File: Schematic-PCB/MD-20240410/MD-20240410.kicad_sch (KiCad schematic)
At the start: 49 parts, among them J1 Conn_01x05_Pin, J2 Conn_01x04_Pin, J3 Conn_01x02_Pin, J4 Conn_01x02_Pin, J5 Conn_01x02_Pin, J6 Conn_01x02_Pin, J7 Conn_01x02_Pin, J8 Conn_01x15_Pin, Q3 NMOS, Q4 NMOS

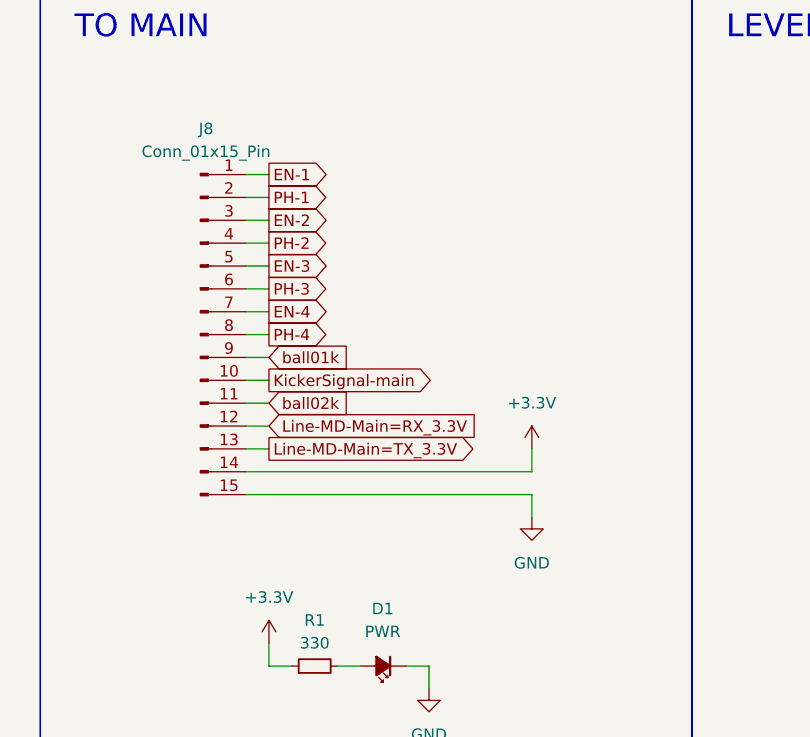
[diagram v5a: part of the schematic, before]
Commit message: FPC/FCCコネクタの順番を変更した
斜めに挿入・逆向きに挿入したときに+3.3VとGNDがショートしないようにした
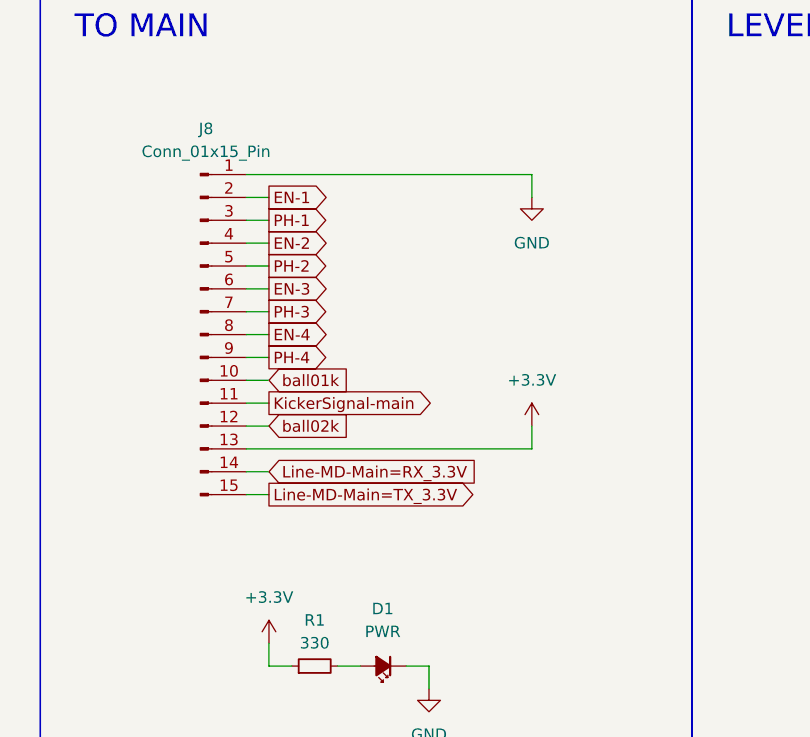
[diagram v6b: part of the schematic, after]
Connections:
- net +3.3V: now also J8.13 (Pin_13); no longer J8.14 (Pin_14)
- net EN-1: now also J8.2 (Pin_2); no longer J8.1 (Pin_1)
- net EN-2: now also J8.4 (Pin_4); no longer J8.3 (Pin_3)
- net EN-3: now also J8.6 (Pin_6); no longer J8.5 (Pin_5)
- net EN-4: now also J8.8 (Pin_8); no longer J8.7 (Pin_7)
- net GND: now also J8.1 (Pin_1); no longer J8.15 (Pin_15)
- net KickerSignal-main: now also J8.11 (Pin_11); no longer J8.10 (Pin_10)
- net Line-MD-Main=RX_3.3V: now also J8.14 (Pin_14); no longer J8.12 (Pin_12)
- net Line-MD-Main=TX_3.3V: now also J8.15 (Pin_15); no longer J8.13 (Pin_13)
- net PH-1: now also J8.3 (Pin_3); no longer J8.2 (Pin_2)
- net PH-2: now also J8.5 (Pin_5); no longer J8.4 (Pin_4)
- net PH-3: now also J8.7 (Pin_7); no longer J8.6 (Pin_6)
- net PH-4: now also J8.9 (Pin_9); no longer J8.8 (Pin_8)
- net ball01k: now also J8.10 (Pin_10); no longer J8.9 (Pin_9)
- net ball02k: now also J8.12 (Pin_12); no longer J8.11 (Pin_11)
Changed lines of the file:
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@@
 	(wire
 		(pts
-			(xy 107.95 179.07) (xy 110.49 179.07)
+			(xy 107.95 181.61) (xy 110.49 181.61)
 		)
 		(stroke
@@
 	(wire
 		(pts
-			(xy 110.49 194.31) (xy 107.95 194.31)
+			(xy 110.49 199.39) (xy 107.95 199.39)
 		)
 		(stroke
@@
 	(wire
 		(pts
-			(xy 107.95 186.69) (xy 110.49 186.69)
+			(xy 107.95 189.23) (xy 110.49 189.23)
 		)
 		(stroke
@@
 	(wire
 		(pts
-			(xy 110.49 166.37) (xy 107.95 166.37)
+			(xy 110.49 168.91) (xy 107.95 168.91)
 		)
 		(stroke
@@
 	(wire
 		(pts
-			(xy 110.49 191.77) (xy 107.95 191.77)
+			(xy 110.49 196.85) (xy 107.95 196.85)
 		)
 		(stroke
@@
 	(wire
 		(pts
-			(xy 107.95 173.99) (xy 110.49 173.99)
+			(xy 107.95 176.53) (xy 110.49 176.53)
 		)
 		(stroke
@@
 	(wire
 		(pts
-			(xy 107.95 168.91) (xy 110.49 168.91)
+			(xy 107.95 171.45) (xy 110.49 171.45)
 		)
 		(stroke
@@
 	(wire
 		(pts
-			(xy 107.95 171.45) (xy 110.49 171.45)
+			(xy 107.95 173.99) (xy 110.49 173.99)
 		)
 		(stroke
@@
 	(wire
 		(pts
-			(xy 107.95 196.85) (xy 139.7 196.85)
+			(xy 107.95 194.31) (xy 139.7 194.31)
 		)
 		(stroke
@@
 	(wire
 		(pts
-			(xy 107.95 184.15) (xy 110.49 184.15)
+			(xy 107.95 186.69) (xy 110.49 186.69)
 		)
 		(stroke
@@
 	(wire
 		(pts
-			(xy 107.95 199.39) (xy 139.7 199.39)
+			(xy 107.95 163.83) (xy 139.7 163.83)
 		)
 		(stroke
@@
 	(wire
 		(pts
-			(xy 139.7 201.93) (xy 139.7 199.39)
+			(xy 139.7 166.37) (xy 139.7 163.83)
 		)
 		(stroke
@@
 	(wire
 		(pts
-			(xy 107.95 176.53) (xy 110.49 176.53)
+			(xy 107.95 179.07) (xy 110.49 179.07)
 		)
 		(stroke
@@
 	(wire
 		(pts
-			(xy 110.49 163.83) (xy 107.95 163.83)
+			(xy 110.49 166.37) (xy 107.95 166.37)
 		)
 		(stroke
@@
 	(wire
 		(pts
-			(xy 107.95 181.61) (xy 110.49 181.61)
+			(xy 107.95 184.15) (xy 110.49 184.15)
 		)
 		(stroke
@@
 	(wire
 		(pts
-			(xy 139.7 196.85) (xy 139.7 194.31)
+			(xy 139.7 194.31) (xy 139.7 191.77)
 		)
 		(stroke
@@
 	(wire
 		(pts
-			(xy 110.49 189.23) (xy 107.95 189.23)
+			(xy 110.49 191.77) (xy 107.95 191.77)
 		)
 		(stroke
@@
 	(global_label "EN-2"
 		(shape output)
-		(at 110.49 168.91 0)
+		(at 110.49 171.45 0)
 		(fields_autoplaced yes)
 		(effects
@@
 		)
 		(property "Intersheetrefs" "${INTERSHEET_REFS}"
-			(at 118.7366 168.91 0)
+			(at 118.7366 171.45 0)
 			(effects
 				(font
@@
 	(global_label "ball02k"
 		(shape input)
-		(at 110.49 189.23 0)
+		(at 110.49 191.77 0)
 		(fields_autoplaced yes)
 		(effects
@@
 		)
 		(property "Intersheetrefs" "${INTERSHEET_REFS}"
-			(at 120.5507 189.23 0)
+			(at 120.5507 191.77 0)
 			(effects
 				(font
@@
 	(global_label "ball01k"
 		(shape input)
-		(at 110.49 184.15 0)
+		(at 110.49 186.69 0)
 		(fields_autoplaced yes)
 		(effects
@@
 		)
 		(property "Intersheetrefs" "${INTERSHEET_REFS}"
-			(at 120.5507 184.15 0)
+			(at 120.5507 186.69 0)
 			(effects
 				(font
@@
 	(global_label "Line-MD-Main=RX_3.3V"
 		(shape input)
-		(at 110.49 191.77 0)
+		(at 110.49 196.85 0)
 		(fields_autoplaced yes)
 		(effects
@@
 		)
 		(property "Intersheetrefs" "${INTERSHEET_REFS}"
-			(at 136.698 191.77 0)
+			(at 136.698 196.85 0)
 			(effects
 				(font
@@
 	(global_label "PH-3"
 		(shape output)
-		(at 110.49 176.53 0)
+		(at 110.49 179.07 0)
 		(fields_autoplaced yes)
 		(effects
@@
 		)
 		(property "Intersheetrefs" "${INTERSHEET_REFS}"
-			(at 118.8576 176.53 0)
+			(at 118.8576 179.07 0)
 			(effects
 				(font
@@
 	(global_label "PH-4"
 		(shape output)
-		(at 110.49 181.61 0)
+		(at 110.49 184.15 0)
 		(fields_autoplaced yes)
 		(effects
@@
 		)
 		(property "Intersheetrefs" "${INTERSHEET_REFS}"
-			(at 118.8576 181.61 0)
+			(at 118.8576 184.15 0)
 			(effects
 				(font
@@
 	(global_label "EN-3"
 		(shape output)
-		(at 110.49 173.99 0)
+		(at 110.49 176.53 0)
 		(fields_autoplaced yes)
 		(effects
@@
 		)
 		(property "Intersheetrefs" "${INTERSHEET_REFS}"
-			(at 118.7366 173.99 0)
+			(at 118.7366 176.53 0)
 			(effects
 				(font
@@
 	(global_label "EN-1"
 		(shape output)
-		(at 110.49 163.83 0)
+		(at 110.49 166.37 0)
 		(fields_autoplaced yes)
 		(effects
@@
 		)
 		(property "Intersheetrefs" "${INTERSHEET_REFS}"
-			(at 118.7366 163.83 0)
+			(at 118.7366 166.37 0)
 			(effects
 				(font
@@
 	(global_label "EN-4"
 		(shape output)
-		(at 110.49 179.07 0)
+		(at 110.49 181.61 0)
 		(fields_autoplaced yes)
 		(effects
@@
 		)
 		(property "Intersheetrefs" "${INTERSHEET_REFS}"
-			(at 118.7366 179.07 0)
+			(at 118.7366 181.61 0)
 			(effects
 				(font
@@
 	(global_label "KickerSignal-main"
 		(shape output)
-		(at 110.49 186.69 0)
+		(at 110.49 189.23 0)
 		(fields_autoplaced yes)
 		(effects
@@
 		)
 		(property "Intersheetrefs" "${INTERSHEET_REFS}"
-			(at 131.4365 186.69 0)
+			(at 131.4365 189.23 0)
 			(effects
 				(font
@@
 	(global_label "Line-MD-Main=TX_3.3V"
 		(shape output)
-		(at 110.49 194.31 0)
+		(at 110.49 199.39 0)
 		(fields_autoplaced yes)
 		(effects
@@
 		)
 		(property "Intersheetrefs" "${INTERSHEET_REFS}"
-			(at 136.3956 194.31 0)
+			(at 136.3956 199.39 0)
 			(effects
 				(font
@@
 	(global_label "PH-1"
 		(shape output)
-		(at 110.49 166.37 0)
+		(at 110.49 168.91 0)
 		(fields_autoplaced yes)
 		(effects
@@
 		)
 		(property "Intersheetrefs" "${INTERSHEET_REFS}"
-			(at 118.8576 166.37 0)
+			(at 118.8576 168.91 0)
 			(effects
 				(font
@@
 	(global_label "PH-2"
 		(shape output)
-		(at 110.49 171.45 0)
+		(at 110.49 173.99 0)
 		(fields_autoplaced yes)
 		(effects
@@
 		)
 		(property "Intersheetrefs" "${INTERSHEET_REFS}"
-			(at 118.8576 171.45 0)
+			(at 118.8576 173.99 0)
 			(effects
 				(font
@@
 	(symbol
 		(lib_id "power:+3.3V")
-		(at 139.7 194.31 0)
+		(at 139.7 191.77 0)
 		(unit 1)
 		(exclude_from_sim no)
@@
 		(dnp no)
 		(property "Reference" "#PWR05"
-			(at 139.7 198.12 0)
+			(at 139.7 195.58 0)
 			(effects
 				(font
@@
 		)
 		(property "Value" "+3.3V"
-			(at 139.7 189.23 0)
+			(at 139.7 186.69 0)
 			(effects
 				(font
@@
 		)
 		(property "Footprint" ""
-			(at 139.7 194.31 0)
+			(at 139.7 191.77 0)
 			(effects
 				(font
@@
 		)
 		(property "Datasheet" ""
-			(at 139.7 194.31 0)
+			(at 139.7 191.77 0)
 			(effects
 				(font
@@
 		)
 		(property "Description" "Power symbol creates a global label with name \"+3.3V\""
-			(at 139.7 194.31 0)
+			(at 139.7 191.77 0)
 			(effects
 				(font
@@
 	(symbol
 		(lib_id "power:GND")
-		(at 139.7 201.93 0)
+		(at 139.7 166.37 0)
 		(unit 1)
 		(exclude_from_sim no)
@@
 		(fields_autoplaced yes)
 		(property "Reference" "#PWR02"
-			(at 139.7 208.28 0)
+			(at 139.7 172.72 0)
 			(effects
 				(font
@@
 		)
 		(property "Value" "GND"
-			(at 139.7 207.01 0)
+			(at 139.7 171.45 0)
 			(effects
 				(font
@@
 		)
 		(property "Footprint" ""
-			(at 139.7 201.93 0)
+			(at 139.7 166.37 0)
 			(effects
 				(font
@@
 		)
 		(property "Datasheet" ""
-			(at 139.7 201.93 0)
+			(at 139.7 166.37 0)
 			(effects
 				(font
@@
 		)
 		(property "Description" "Power symbol creates a global label with name \"GND\" , ground"
-			(at 139.7 201.93 0)
+			(at 139.7 166.37 0)
 			(effects
 				(font

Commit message: update: MD基板の回路図を開いた
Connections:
- net Line-MD-Main=RX_3.3V renamed Line-Main=RX_3.3V
- net Line-MD-Main=RX_5V renamed Line-Main=RX_5V
- net Line-MD-Main=TX_3.3V renamed Line-Main=TX_3.3V
- net Line-MD-Main=TX_5V renamed Line-Main=TX_5V
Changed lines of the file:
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@@
 		)
 	)
-	(global_label "Line-MD-Main=TX_3.3V"
+	(global_label "Line-Main=TX_3.3V"
 		(shape input)
 		(at 199.39 210.82 180)
@@
 		)
 	)
-	(global_label "Line-MD-Main=RX_3.3V"
+	(global_label "Line-Main=RX_3.3V"
 		(shape input)
 		(at 110.49 196.85 0)
@@
 		)
 	)
-	(global_label "Line-MD-Main=RX_3.3V"
+	(global_label "Line-Main=RX_3.3V"
 		(shape output)
 		(at 200.66 186.69 180)
@@
 		)
 	)
-	(global_label "Line-MD-Main=TX_5V"
+	(global_label "Line-Main=TX_5V"
 		(shape output)
 		(at 245.11 210.82 0)
@@
 		)
 	)
-	(global_label "Line-MD-Main=RX_5V"
+	(global_label "Line-Main=RX_5V"
 		(shape output)
 		(at 41.91 264.16 0)
@@
 		)
 	)
-	(global_label "Line-MD-Main=RX_5V"
+	(global_label "Line-Main=RX_5V"
 		(shape input)
 		(at 245.11 186.69 0)
@@
 		)
 	)
-	(global_label "Line-MD-Main=TX_3.3V"
+	(global_label "Line-Main=TX_3.3V"
 		(shape output)
 		(at 110.49 199.39 0)
@@
 		)
 	)
-	(global_label "Line-MD-Main=TX_5V"
+	(global_label "Line-Main=TX_5V"
 		(shape input)
 		(at 41.91 261.62 0)

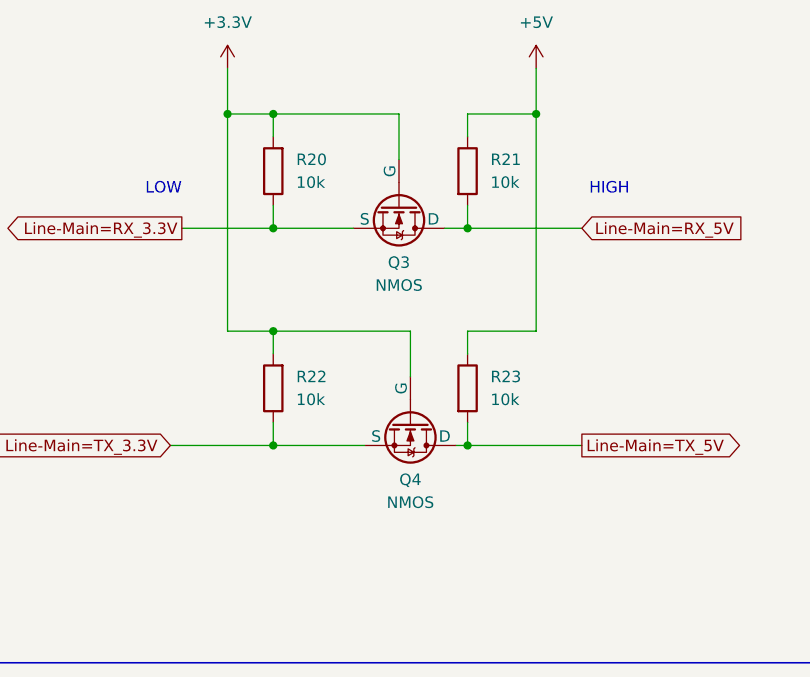
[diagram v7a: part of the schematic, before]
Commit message: update: MD基板のNchMOSFET部分の設計を修正した
ピンアサインも確認したから大丈夫だと思う
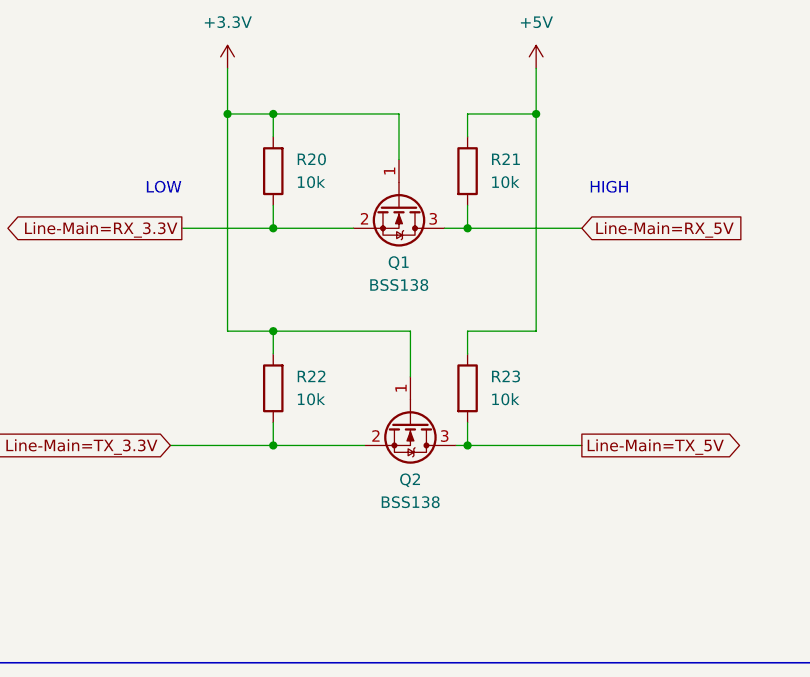
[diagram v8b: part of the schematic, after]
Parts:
- removed Q3, Q4: NMOS, Package_TO_SOT_SMD:SOT-23, symbol Simulation_SPICE:NMOS
- added Q1, Q2: BSS138, Package_TO_SOT_SMD:SOT-23, symbol Transistor_FET:BSS138
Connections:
- net +3.3V: now also Q1.1 (G), Q2.1 (G)
- net Line-Main=RX_3.3V: now also Q1.2 (S)
- net Line-Main=RX_5V: now also Q1.3 (D)
- net Line-Main=TX_3.3V: now also Q2.2 (S)
- net Line-Main=TX_5V: now also Q2.3 (D)
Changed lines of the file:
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@@
 	)
 	(symbol
+		(lib_id "Transistor_FET:BSS138")
+		(at 226.06 208.28 270)
+		(unit 1)
+		(exclude_from_sim no)
+		(in_bom yes)
+		(on_board yes)
+		(dnp no)
+		(fields_autoplaced yes)
+		(property "Reference" "Q2"
+			(at 226.06 214.63 90)
+			(effects
+				(font
+					(size 1.27 1.27)
+				)
+			)
+		)
+		(property "Value" "BSS138"
+			(at 226.06 217.17 90)
+			(effects
+				(font
+					(size 1.27 1.27)
+				)
+			)
+		)
+		(property "Footprint" "Package_TO_SOT_SMD:SOT-23"
+			(at 224.155 213.36 0)
+			(effects
+				(font
+					(size 1.27 1.27)
+					(italic yes)
+				)
+				(justify left)
+				(hide yes)
+			)
+		)
+		(property "Datasheet" "https://www.onsemi.com/pub/Collateral/BSS138-D.PDF"
+			(at 222.25 213.36 0)
+			(effects
+				(font
+					(size 1.27 1.27)
+				)
+				(justify left)
+				(hide yes)
+			)
+		)
+		(property "Description" "50V Vds, 0.22A Id, N-Channel MOSFET, SOT-23"
+			(at 226.06 208.28 0)
+			(effects
+				(font
+					(size 1.27 1.27)
+				)
+				(hide yes)
+			)
+		)
+		(pin "1"
+		)
+		(pin "3"
+		)
+		(pin "2"
+		)
+		(instances
+			(project "MD-20240410"
+				(path "/bcc67a42-c6e5-4887-87e7-f99f98dfab76"
+					(reference "Q2")
+					(unit 1)
+				)
+			)
+		)
+	)
+	(symbol
 		(lib_id "@2024TOINIOT2-MD:DRV8874")
 		(at 198.12 27.94 0)
@@
 	)
 	(symbol
-		(lib_id "Simulation_SPICE:NMOS")
-		(at 224.79 184.15 270)
-		(unit 1)
-		(exclude_from_sim no)
-		(in_bom yes)
-		(on_board yes)
-		(dnp no)
-		(fields_autoplaced yes)
-		(property "Reference" "Q3"
-			(at 224.79 190.5 90)
-			(effects
-				(font
-					(size 1.27 1.27)
-				)
-			)
-		)
-		(property "Value" "NMOS"
-			(at 224.79 193.04 90)
-			(effects
-				(font
-					(size 1.27 1.27)
-				)
-			)
-		)
-		(property "Footprint" "Package_TO_SOT_SMD:SOT-23"
-			(at 227.33 189.23 0)
-			(effects
-				(font
-					(size 1.27 1.27)
-				)
-				(hide yes)
-			)
-		)
-		(property "Datasheet" "https://ngspice.sourceforge.io/docs/ngspice-html-manual/manual.xhtml#cha_MOSFETs"
-			(at 212.09 184.15 0)
-			(effects
-				(font
-					(size 1.27 1.27)
-				)
-				(hide yes)
-			)
-		)
-		(property "Description" "N-MOSFET transistor, drain/source/gate"
-			(at 224.79 184.15 0)
-			(effects
-				(font
-					(size 1.27 1.27)
-				)
-				(hide yes)
-			)
-		)
-		(property "Sim.Device" "NMOS"
-			(at 207.645 184.15 0)
-			(effects
-				(font
-					(size 1.27 1.27)
-				)
-				(hide yes)
-			)
-		)
-		(property "Sim.Type" "VDMOS"
-			(at 205.74 184.15 0)
-			(effects
-				(font
-					(size 1.27 1.27)
-				)
-				(hide yes)
-			)
-		)
-		(property "Sim.Pins" "1=D 2=G 3=S"
-			(at 209.55 184.15 0)
-			(effects
-				(font
-					(size 1.27 1.27)
-				)
-				(hide yes)
-			)
-		)
-		(pin "2"
-		)
-		(pin "3"
-		)
-		(pin "1"
-		)
-		(instances
-			(project "MD-20240410"
-				(path "/bcc67a42-c6e5-4887-87e7-f99f98dfab76"
-					(reference "Q3")
-					(unit 1)
-				)
-			)
-		)
-	)
-	(symbol
 		(lib_id "Device:R")
 		(at 160.02 120.65 0)
@@
 	)
 	(symbol
-		(lib_id "Simulation_SPICE:NMOS")
-		(at 226.06 208.28 270)
-		(unit 1)
-		(exclude_from_sim no)
-		(in_bom yes)
-		(on_board yes)
-		(dnp no)
-		(fields_autoplaced yes)
-		(property "Reference" "Q4"
-			(at 226.06 214.63 90)
-			(effects
-				(font
-					(size 1.27 1.27)
-				)
-			)
-		)
-		(property "Value" "NMOS"
-			(at 226.06 217.17 90)
-			(effects
-				(font
-					(size 1.27 1.27)
-				)
-			)
-		)
-		(property "Footprint" "Package_TO_SOT_SMD:SOT-23"
-			(at 228.6 213.36 0)
-			(effects
-				(font
-					(size 1.27 1.27)
-				)
-				(hide yes)
-			)
-		)
-		(property "Datasheet" "https://ngspice.sourceforge.io/docs/ngspice-html-manual/manual.xhtml#cha_MOSFETs"
-			(at 213.36 208.28 0)
-			(effects
-				(font
-					(size 1.27 1.27)
-				)
-				(hide yes)
-			)
-		)
-		(property "Description" "N-MOSFET transistor, drain/source/gate"
-			(at 226.06 208.28 0)
-			(effects
-				(font
-					(size 1.27 1.27)
-				)
-				(hide yes)
-			)
-		)
-		(property "Sim.Device" "NMOS"
-			(at 208.915 208.28 0)
-			(effects
-				(font
-					(size 1.27 1.27)
-				)
-				(hide yes)
-			)
-		)
-		(property "Sim.Type" "VDMOS"
-			(at 207.01 208.28 0)
-			(effects
-				(font
-					(size 1.27 1.27)
-				)
-				(hide yes)
-			)
-		)
-		(property "Sim.Pins" "1=D 2=G 3=S"
-			(at 210.82 208.28 0)
-			(effects
-				(font
-					(size 1.27 1.27)
-				)
-				(hide yes)
-			)
-		)
-		(pin "2"
-		)
-		(pin "3"
-		)
-		(pin "1"
-		)
-		(instances
-			(project "MD-20240410"
-				(path "/bcc67a42-c6e5-4887-87e7-f99f98dfab76"
-					(reference "Q4")
-					(unit 1)
-				)
-			)
-		)
-	)
-	(symbol
 		(lib_id "power:GND")
 		(at 198.12 67.31 0)
@@
 					(unit 1)
 				)
+			)
+		)
+	)
+	(symbol
+		(lib_id "Transistor_FET:BSS138")
+		(at 224.79 184.15 270)
+		(unit 1)
+		(exclude_from_sim no)
+		(in_bom yes)
+		(on_board yes)
+		(dnp no)
+		(fields_autoplaced yes)
+		(property "Reference" "Q1"
+			(at 224.79 190.5 90)
+			(effects
+				(font
+					(size 1.27 1.27)
+				)
+			)
+		)
+		(property "Value" "BSS138"
+			(at 224.79 193.04 90)
+			(effects
+				(font
+					(size 1.27 1.27)
+				)
+			)
+		)
+		(property "Footprint" "Package_TO_SOT_SMD:SOT-23"
+			(at 222.885 189.23 0)
+			(effects
+				(font
+					(size 1.27 1.27)
+					(italic yes)
+				)
+				(justify left)
+				(hide yes)
+			)
+		)
+		(property "Datasheet" "https://www.onsemi.com/pub/Collateral/BSS138-D.PDF"
+			(at 220.98 189.23 0)
+			(effects
+				(font
+					(size 1.27 1.27)
+				)
+				(justify left)
+				(hide yes)
+			)
+		)
+		(property "Description" "50V Vds, 0.22A Id, N-Channel MOSFET, SOT-23"
+			(at 224.79 184.15 0)
+			(effects
+				(font
+					(size 1.27 1.27)
+				)
+				(hide yes)
+			)
+		)
+		(pin "1"
+		)
+		(pin "3"
+		)
+		(pin "2"
+		)
+		(instances
+			(project "MD-20240410"
+				(path "/bcc67a42-c6e5-4887-87e7-f99f98dfab76"
+					(reference "Q1")
+					(unit 1)
+				)
